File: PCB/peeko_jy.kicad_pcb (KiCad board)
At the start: 4 copper layers, 52.1 x 45.7 mm, 60 parts, among them J1 Rasberry PI Pico, J2 Conn_02x15_Odd_Even, J3 Conn_01x02_Pin, J4 Conn_01x02_Pin

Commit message: jy inner2 5v
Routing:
- net +5V: track 76.0 -> 76.5 mm

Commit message: jy reduce from 4 layer to 2
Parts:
- moved REF** 2.11 mm to (161.9, 108.8) (x2)
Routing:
- net +3V3: track 129.4 -> 215.5 mm
- net +5V: track 76.5 -> 82.5 mm
- net /CHAIN: track 85.9 -> 85.1 mm
- net GND: vias 44 -> 124
- removed copper zone on In1.Cu, net GND
- removed copper zone on In2.Cu, net GND
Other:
- copper layers 4 -> 2

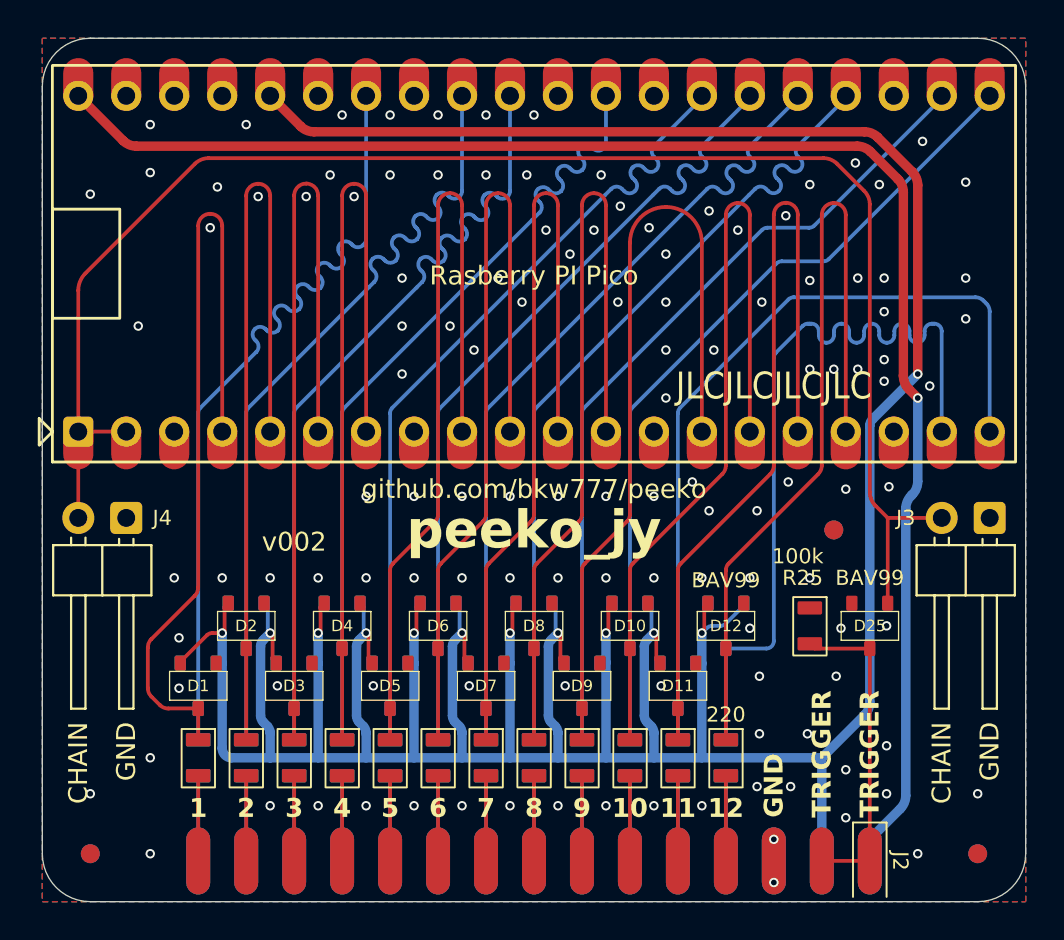
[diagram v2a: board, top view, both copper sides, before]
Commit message: jy ground paths, jy housing
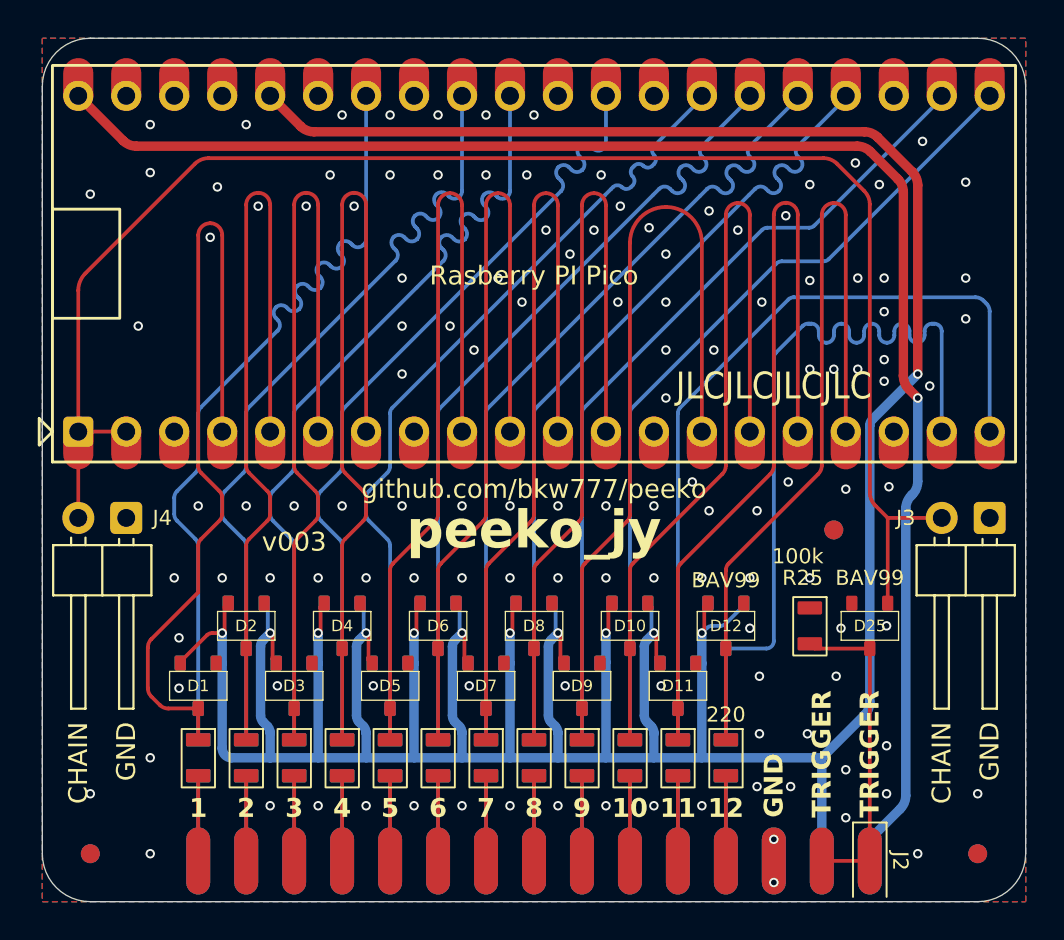
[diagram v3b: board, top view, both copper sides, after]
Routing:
- net GND: vias 124 -> 127
